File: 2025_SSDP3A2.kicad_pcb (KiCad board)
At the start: 4 copper layers, 58.4 x 28.8 mm, 61 parts, among them J1 SolderPad, J2 SolderPad, J3 SolderPad, J4 SolderPad, Q1 CSD19534Q5A, Q2 BSC0805LS, U1 LM5146RGYR

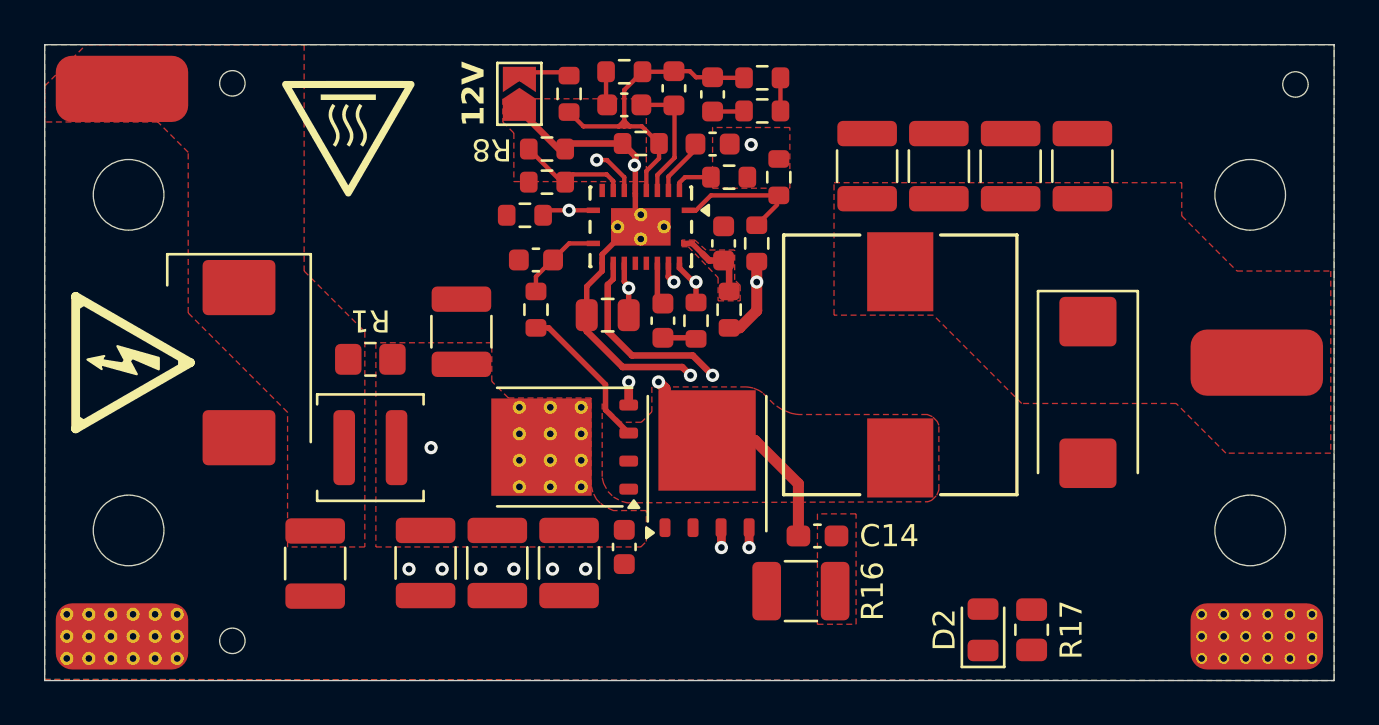
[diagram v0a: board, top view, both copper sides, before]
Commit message: Using PQFN FETs instead of SuperSO-8
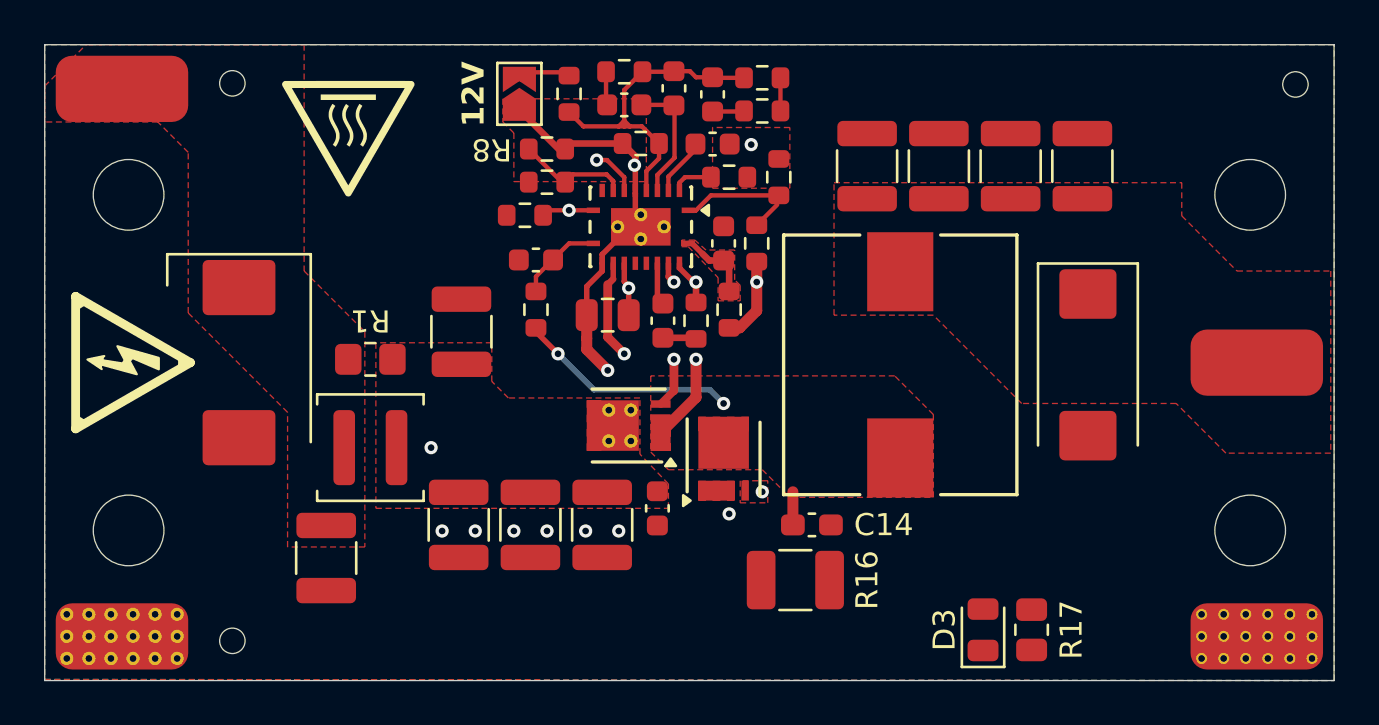
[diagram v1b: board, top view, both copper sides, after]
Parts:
- C15: value 18pF -> 12pF
- Q1: value CSD19534Q5A -> IAUZ30N10S5L240; footprint Package_TO_SOT_SMD:TDSON-8-1 -> TSDSON-8:PG-TSDSON-8-26_TV
- Q2: value BSC0805LS -> BSZ096N10LS5; footprint Package_TO_SOT_SMD:TDSON-8-1 -> TSDSON-8:PG-TSDSON-8-26
- R15: value 330 -> 360
- moved Q1 3.06 mm to (146.4, 117.2)
- moved C1 2.30 mm to (147.8, 121.0)
- moved C2 2.29 mm to (138.8, 121.8)
- moved C3 2.29 mm to (142.0, 121.8)
- moved C4 2.29 mm to (145.2, 121.8)
- moved C20 1.25 mm to (167.2, 114.5)
- moved Q2 0.78 mm to (150.8, 118.8)
- moved C14 0.56 mm to (154.8, 121.8)
- moved C6 0.56 mm to (132.8, 123.2)
- moved R16 0.56 mm to (154.0, 124.2)
- renumbered D2 to D3
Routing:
- net /LO: track 18.2 -> 13.5 mm
- net /SW: track 24.8 -> 21.2 mm, vias 2 -> 4
- net PGND: track 21.0 -> 17.5 mm
- added copper zone on F.Cu, net /LO
- removed copper zone on F.Cu, net /SNUB_RC

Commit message: Finished routing
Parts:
- R7: value 27k -> 24k
- moved D3 1.50 mm to (161.0, 126.5)
- moved R17 1.50 mm to (163.2, 126.5)
- moved L1 1.00 mm to (134.8, 117.2)
- moved R1 1.00 mm to (134.8, 113.2)
- moved C6 0.75 mm to (132.8, 122.5)
- moved C5 0.28 mm to (138.8, 112.8)
- moved C20 0.25 mm to (167.5, 114.5)
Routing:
- net VOUT: track 1.50 -> 18.6 mm, vias 0 -> 2
- net VCC: track 2.43 -> 12.2 mm, vias 1 -> 2
- net /SW: track 21.2 -> 25.7 mm
- net VIN: track 22.5 -> 21.7 mm
- net PGND: track 17.5 -> 17.7 mm, vias 8 -> 86
- added copper zone on F.Cu, net /SNUB_RC

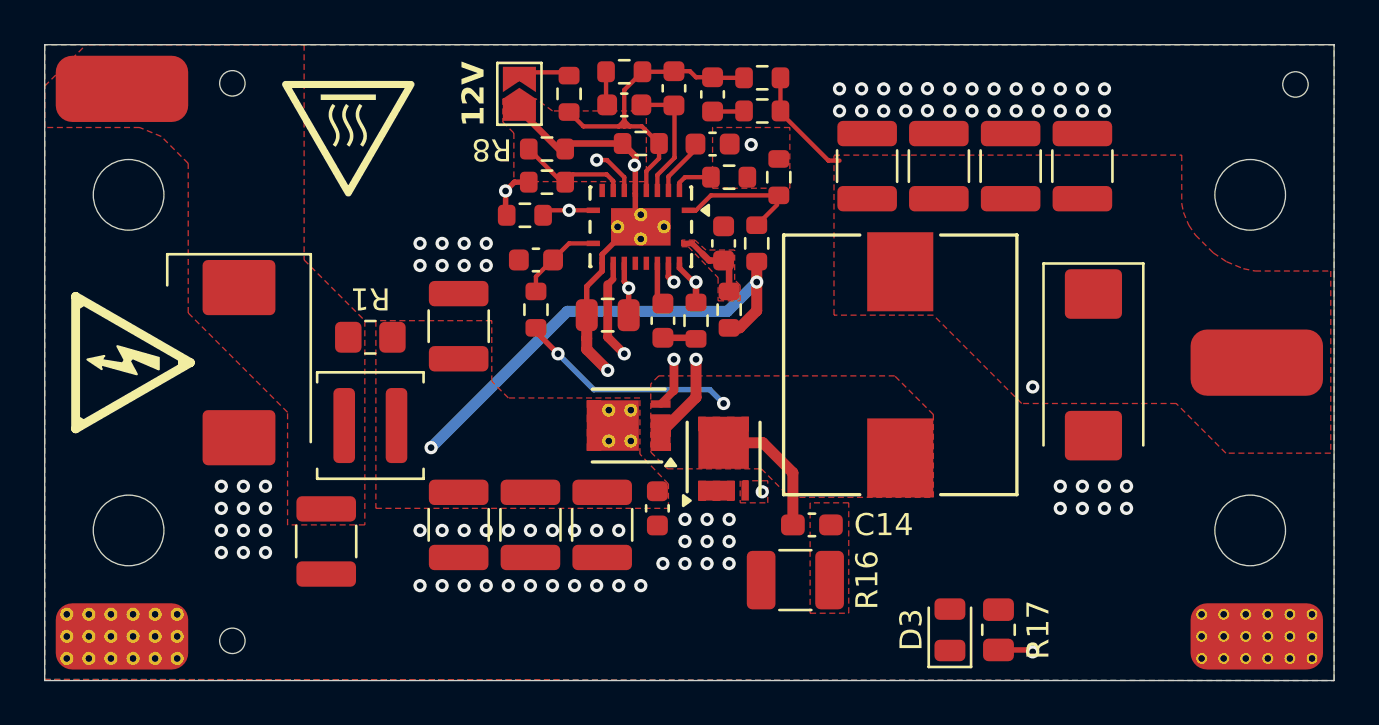
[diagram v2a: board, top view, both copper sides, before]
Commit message: Added silkscreen markings, tweaked routing
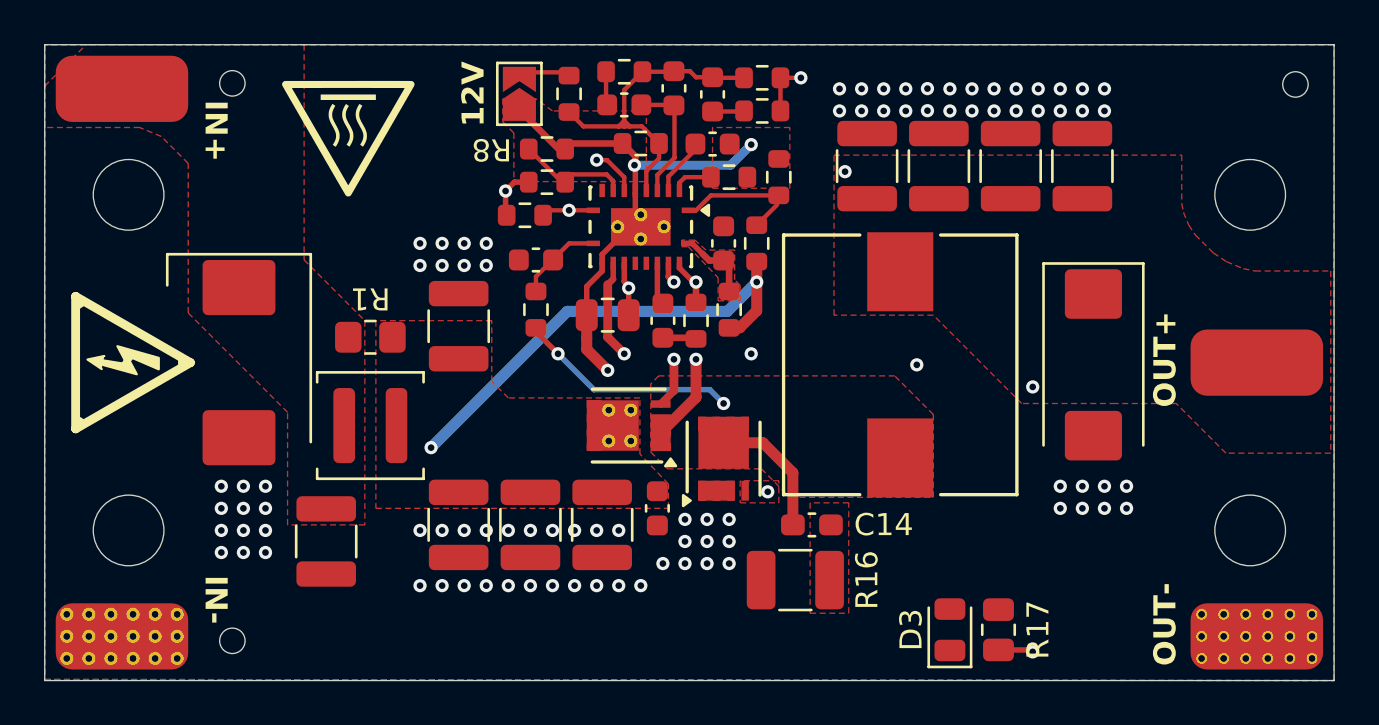
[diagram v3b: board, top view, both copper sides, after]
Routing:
- net VOUT: track 18.6 -> 21.0 mm, vias 2 -> 4
- net PGND: vias 86 -> 88
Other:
- board text added: "IN+"
- board text added: "IN-"
- board text added: "OUT+"
- board text added: "OUT-"
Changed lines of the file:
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@@
 		(layer "Edge.Cuts")
+	)
+	(gr_text "OUT+"
+		(at 170.75 114.25 90)
+		(layer "F.SilkS")
+		(effects
+			(font
+				(size 1 1)
+				(thickness 0.2)
+				(bold yes)
+			)
+		)
+	)
+	(gr_text "IN+"
+		(at 127.75 102.5 270)
+		(layer "F.SilkS")
+		(effects
+			(font
+				(size 1 1)
+				(thickness 0.2)
+				(bold yes)
+			)
+			(justify left)
+		)
+	)
+	(gr_text "IN-"
+		(at 127.75 126.25 270)
+		(layer "F.SilkS")
+		(effects
+			(font
+				(size 1 1)
+				(thickness 0.2)
+				(bold yes)
+			)
+			(justify right)
+		)
+	)
+	(gr_text "OUT-"
+		(at 170.75 126.25 90)
+		(layer "F.SilkS")
+		(effects
+			(font
+				(size 1 1)
+				(thickness 0.2)
+				(bold yes)
+			)
+		)
 	)
 	(gr_text "12V"
@@
 	)
 	(via
+		(at 152 114)
+		(size 0.6)
+		(drill 0.3)
+		(layers "F.Cu" "B.Cu")
+		(free yes)
+		(net 1)
+	)
+	(via
 		(at 138 124.5)
 		(size 0.6)
@@
 	(via
 		(at 165 102)
+		(size 0.6)
+		(drill 0.3)
+		(layers "F.Cu" "B.Cu")
+		(free yes)
+		(net 1)
+	)
+	(via
+		(at 159.5 114.5)
 		(size 0.6)
 		(drill 0.3)
@@
 	)
 	(segment
+		(start 146.713343 105.456671)
+		(end 151.068329 105.456671)
+		(width 0.4)
+		(layer "B.Cu")
+		(net 3)
+	)
+	(segment
 		(start 151.068329 105.456671)
-		(end 146.713343 105.456671)
-		(width 0.5)
-		(layer "In2.Cu")
-		(net 3)
-	)
-	(segment
-		(start 152 104.525)
-		(end 151.068329 105.456671)
-		(width 0.5)
-		(layer "In2.Cu")
+		(end 152 104.525)
+		(width 0.4)
+		(layer "B.Cu")
 		(net 3)
 	)
@@
 	)
 	(segment
-		(start 153.325 103.075)
-		(end 155.5 105.25)
+		(start 153.325 101.5)
+		(end 154.25 101.5)
 		(width 0.2)
 		(layer "F.Cu")
@@
 	)
 	(segment
-		(start 155.5 105.25)
-		(end 156 105.25)
-		(width 0.2)
-		(layer "F.Cu")
-		(net 12)
-	)
-	(segment
 		(start 163.2 127.4125)
 		(end 164.6625 127.4125)
@@
 	)
 	(via
+		(at 154.25 101.5)
+		(size 0.6)
+		(drill 0.3)
+		(layers "F.Cu" "B.Cu")
+		(net 12)
+	)
+	(via
+		(at 156.25 105.75)
+		(size 0.6)
+		(drill 0.3)
+		(layers "F.Cu" "B.Cu")
+		(net 12)
+	)
+	(via
 		(at 164.75 127.5)
 		(size 0.6)
 		(drill 0.3)
 		(layers "F.Cu" "B.Cu")
+		(net 12)
+	)
+	(segment
+		(start 154.25 103.75)
+		(end 156.25 105.75)
+		(width 0.2)
+		(layer "In2.Cu")
 		(net 12)
 	)
@@
 		(end 164.75 115.5)
 		(width 0.25)
+		(layer "In2.Cu")
+		(net 12)
+	)
+	(segment
+		(start 154.25 101.5)
+		(end 154.25 103.75)
+		(width 0.2)
 		(layer "In2.Cu")
 		(net 12)
@@
 	)
 	(via
-		(at 152.5 120.25)
+		(at 152.75 120.25)
 		(size 0.6)
 		(drill 0.3)
@@
 	)
 	(segment
-		(start 152.5 120)
-		(end 152.5 120.25)
+		(start 146.5 114)
+		(end 146.25 114)
 		(width 0.5)
 		(layer "In2.Cu")
@@
 	)
 	(segment
-		(start 146.25 114)
+		(start 152.75 120.25)
 		(end 146.5 114)
-		(width 0.5)
-		(layer "In2.Cu")
-		(net 17)
-	)
-	(segment
-		(start 146.5 114)
-		(end 152.5 120)
 		(width 0.5)
 		(layer "In2.Cu")
@@
 		(polygon
 			(pts
-				(xy 151.5 119.75) (xy 151.5 120.75) (xy 152.75 120.75) (xy 152.75 119.75)
+				(xy 151.5 119.75) (xy 151.5 120.75) (xy 153.25 120.75) (xy 153.25 119.75)
 			)
 		)

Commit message: Tweaked routing, changed some fab parameters
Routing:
- net /HO: track 7.75 -> 6.75 mm
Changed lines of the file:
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@@
 			)
 		)
-		(property "FT Rotation Offset" "-90"
+		(property "FT Rotation Offset" "0"
 			(at 0 0 90)
 			(unlocked yes)
@@
 			)
 		)
-		(property "FT Rotation Offset" "-90"
+		(property "FT Rotation Offset" "0"
 			(at 0 0 180)
 			(unlocked yes)
@@
 			)
 		)
-		(property "FT Rotation Offset" "-90"
+		(property "FT Rotation Offset" "0"
 			(at 0 0 270)
 			(unlocked yes)
@@
 	)
 	(segment
-		(start 148.5 114.25)
-		(end 148.5 113.25)
-		(width 0.4)
-		(layer "In2.Cu")
-		(net 14)
-	)
-	(segment
 		(start 148.5 110.75)
 		(end 148.5 114.25)
@@
 		(start 149.5 114.25)
 		(end 149.5 115.975)
-		(width 0.5)
+		(width 0.4)
 		(layer "F.Cu")
 		(net 15)

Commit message: Tweaked routing
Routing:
- net PGND: vias 88 -> 90
- added copper zone on F.Cu, net /HO
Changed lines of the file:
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@@
+	)
+	(via
+		(at 152 121.499048)
+		(size 0.6)
+		(drill 0.3)
+		(layers "F.Cu" "B.Cu")
+		(net 1)
 	)
 	(via
@@
 	(via
 		(at 144 124.5)
+		(size 0.6)
+		(drill 0.3)
+		(layers "F.Cu" "B.Cu")
+		(free yes)
+		(net 1)
+	)
+	(via
+		(at 152 122.5)
 		(size 0.6)
 		(drill 0.3)
@@
 	)
 	(segment
-		(start 148.5 114.25)
-		(end 148.5 115.675)
-		(width 0.4)
-		(layer "F.Cu")
-		(net 14)
-	)
-	(segment
-		(start 148.5 114.25)
-		(end 148.475 114.25)
+		(start 148.5 114.5)
+		(end 148.475 114.475)
 		(width 0.4)
 		(layer "F.Cu")
@@
 		(net 14)
 	)
+	(segment
+		(start 148.5 114.5)
+		(end 148.5 115.675)
+		(width 0.4)
+		(layer "F.Cu")
+		(net 14)
+	)
 	(via
 		(at 148.5 110.75)
@@
 	)
 	(via
-		(at 148.5 114.25)
+		(at 148.5 114.5)
 		(size 0.6)
 		(drill 0.3)
@@
 	(segment
 		(start 148.5 110.75)
-		(end 148.5 114.25)
+		(end 148.5 114.5)
 		(width 0.5)
 		(layer "In2.Cu")
@@
 	)
 	(segment
+		(start 148.55 117.575)
+		(end 147.9 117.575)
+		(width 0.5)
+		(layer "F.Cu")
+		(net 15)
+	)
+	(segment
 		(start 153.8875 121.75)
 		(end 153.8875 119.3875)
@@
 	(segment
 		(start 147.9 117.55)
-		(end 147.9 117.575)
-		(width 0.5)
-		(layer "F.Cu")
-		(net 15)
-	)
-	(segment
-		(start 149.5 114.25)
-		(end 149.5 115.975)
-		(width 0.4)
-		(layer "F.Cu")
-		(net 15)
-	)
-	(segment
-		(start 149.5 115.975)
 		(end 147.9 117.575)
 		(width 0.5)
@@
 	)
 	(segment
+		(start 149.5 116.625)
+		(end 148.55 117.575)
+		(width 0.5)
+		(layer "F.Cu")
+		(net 15)
+	)
+	(segment
+		(start 149.5 115.975)
+		(end 149.5 116.625)
+		(width 0.5)
+		(layer "F.Cu")
+		(net 15)
+	)
+	(segment
+		(start 149.5 114.5)
+		(end 149.5 115.975)
+		(width 0.4)
+		(layer "F.Cu")
+		(net 15)
+	)
+	(segment
 		(start 142.25 113)
 		(end 143.25 114)
@@
 	)
 	(via
-		(at 149.5 114.25)
+		(at 149.5 114.5)
 		(size 0.6)
 		(drill 0.3)
@@
 	(segment
 		(start 149.5 110.75)
-		(end 149.5 114.25)
+		(end 149.5 114.5)
 		(width 0.5)
 		(layer "In2.Cu")
@@
 	)
 	(segment
+		(start 146.25 114)
+		(end 145.5 113.25)
+		(width 0.4)
+		(layer "F.Cu")
+		(net 17)
+	)
+	(segment
 		(start 145.5 113.25)
-		(end 146.25 114)
-		(width 0.4)
-		(layer "F.Cu")
-		(net 17)
-	)
-	(segment
-		(start 145.5 110.864702)
-		(end 145.5 113.25)
+		(end 145.5 110.864702)
 		(width 0.4)
 		(layer "F.Cu")
@@
 	)
 	(segment
-		(start 146.5 114)
-		(end 146.25 114)
+		(start 146.25 114)
+		(end 146.5 114)
 		(width 0.5)
 		(layer "In2.Cu")
@@
 	)
 	(segment
-		(start 152.75 120.25)
-		(end 146.5 114)
+		(start 146.5 114)
+		(end 152.75 120.25)
 		(width 0.5)
 		(layer "In2.Cu")
@@
 				(xy 171.579101 107.594347) (xy 171.816406 108.167251) (xy 172.116756 108.616756) (xy 172.927659 109.427659)
 				(xy 173.526998 109.828125) (xy 174.290871 110.144531) (xy 174.821098 110.25) (xy 178.25 110.25)
-				(xy 178.25 118.5) (xy 173.5 118.5) (xy 171.25 116.25) (xy 168.5 116.25)
+				(xy 178.25 118.75) (xy 173.75 118.75) (xy 171.25 116.25) (xy 168.5 116.25)
 			)
 		)
@@
 				(xy 135 112.5) (xy 135 121) (xy 148.25 121) (xy 148.25 119.895355) (xy 146.96 118.545356) (xy 146.96 116)
 				(xy 141 116) (xy 140.25 115.25) (xy 140.25 112.5)
+			)
+		)
+	)
+	(zone
+		(net 15)
+		(net_name "/SW")
+		(layer "F.Cu")
+		(name "TZSWCC")
+		(hatch edge 0.5)
+		(priority 9)
+		(connect_pads yes
+			(clearance 0.25)
+		)
+		(min_thickness 0.25)
+		(filled_areas_thickness no)
+		(fill yes
+			(thermal_gap 0.5)
+			(thermal_bridge_width 0.5)
+		)
+		(polygon
+			(pts
+				(xy 147.5 115) (xy 149.75 115) (xy 149.75 118.25) (xy 147.5 118.25)
 			)
 		)
@@
 			)
 		)
+	)
+	(zone
+		(net 14)
+		(net_name "/HO")
+		(layer "F.Cu")
+		(name "TZHO")
+		(hatch edge 0.5)
+		(priority 10)
+		(connect_pads yes
+			(clearance 0.25)
+		)
+		(min_thickness 0.25)
+		(filled_areas_thickness no)
+		(fill yes
+			(thermal_gap 0.5)
+			(thermal_bridge_width 0.5)
+		)
+		(polygon
+			(pts
+				(xy 148.25 114) (xy 148.25 115) (xy 147.45 115.8) (xy 147.45 116.5) (xy 148.3 116.5) (xy 148.75 116.05)
+				(xy 148.75 114)
+			)
+		)
